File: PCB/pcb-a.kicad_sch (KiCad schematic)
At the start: 24 parts, among them Q3 BC337, Q4 BC337, SW1 config, U1 MCP23008-xP, U4 ATmega16L-8P, Y1 8Mhz

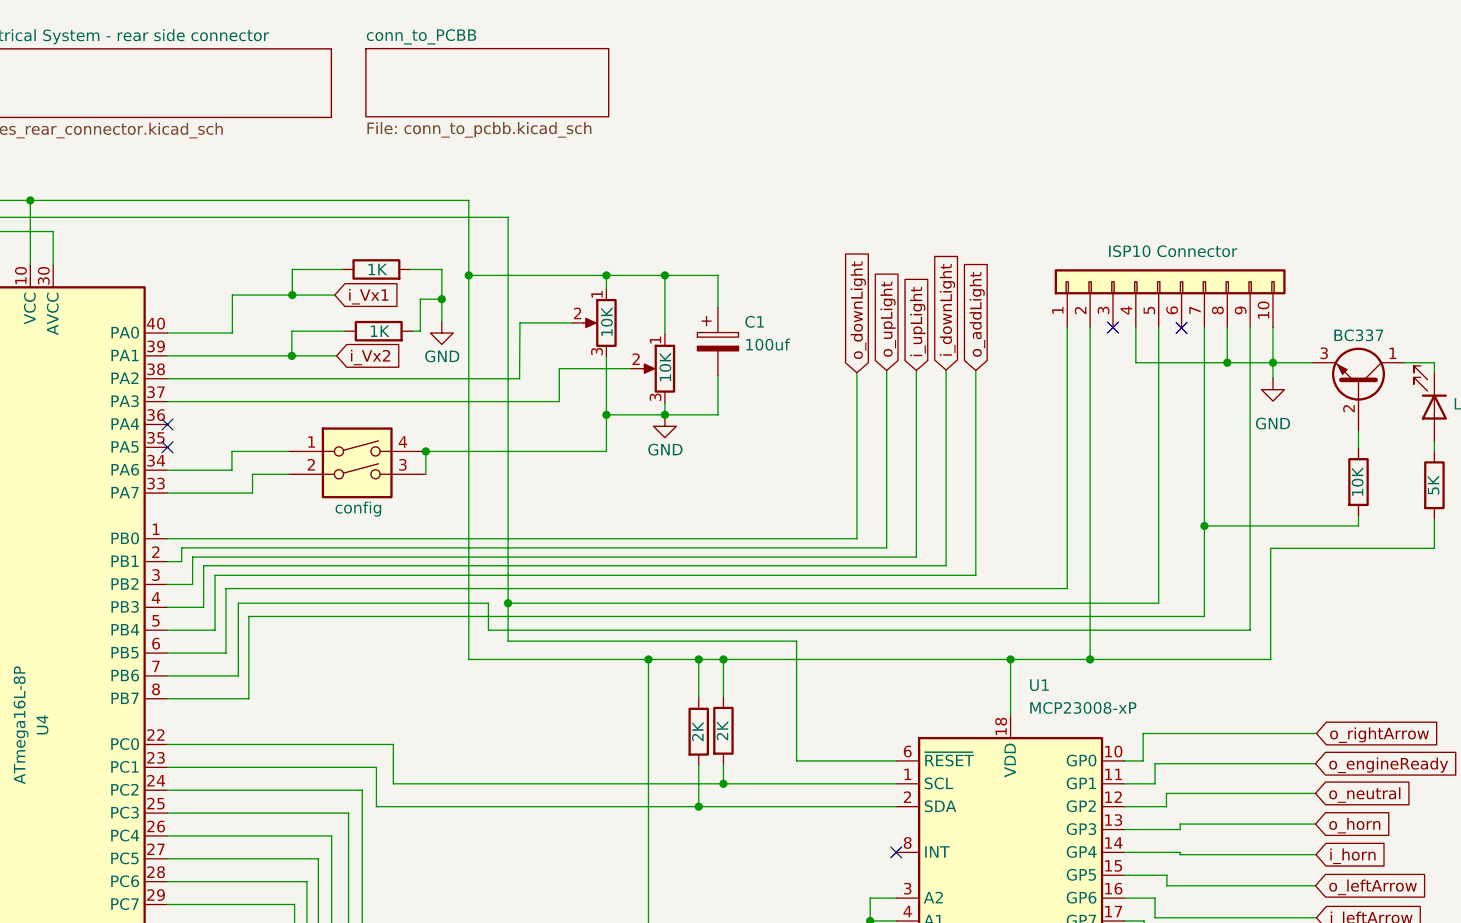
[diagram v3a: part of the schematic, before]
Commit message: Changes and porting to KiCAD-7.0
The MCP23008's reset PIN is no more connected to the MCU's reset. Now, it is connected to the A4 MCU's pin.
This change allows the MCU to reset the I2C connected device, when there are too many errors
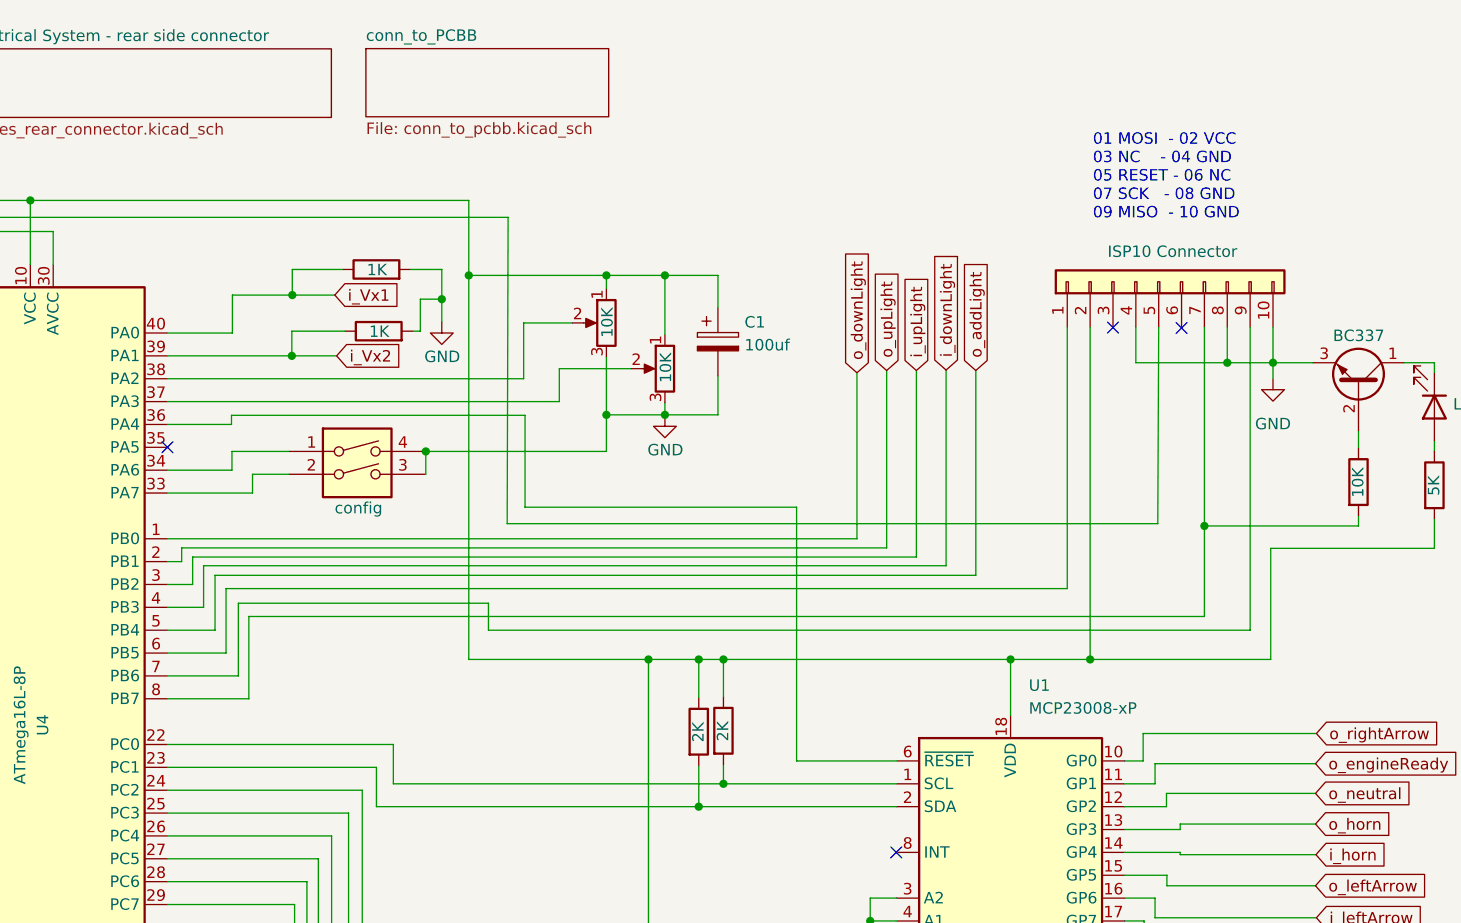
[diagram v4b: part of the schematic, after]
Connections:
- net i_powerOFF: no longer U1.6 (~{RESET})
- net at U4.36 (PA4): now also U1.6 (~{RESET})
- no-connect marks 7 -> 6
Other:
- note added: "01 MOSI - 02 VCC 03 NC - 04 GND 05 RESET - 06 NC 07 SCK - 08 GND 09 MISO - 10 GND"

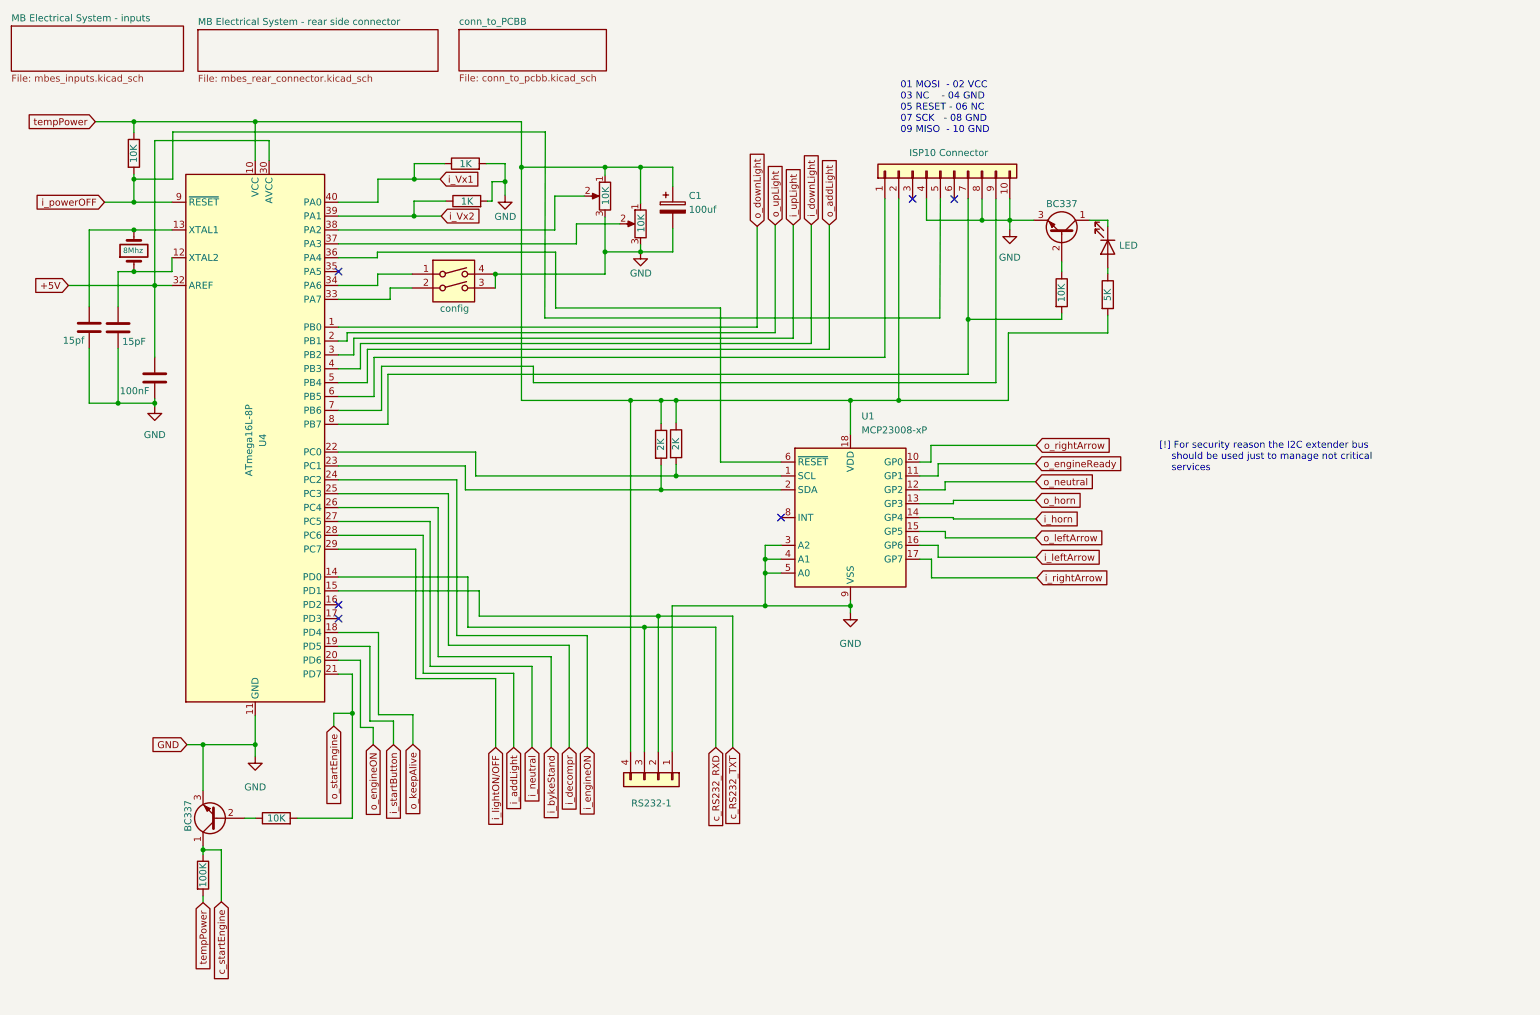
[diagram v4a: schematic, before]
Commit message: MAX232CPE added
In order to see the log messages when the device is mounted on motobike, I need to put the RS232 plug into the device directly.
For this reason I added the RS232 transciver to the circuit
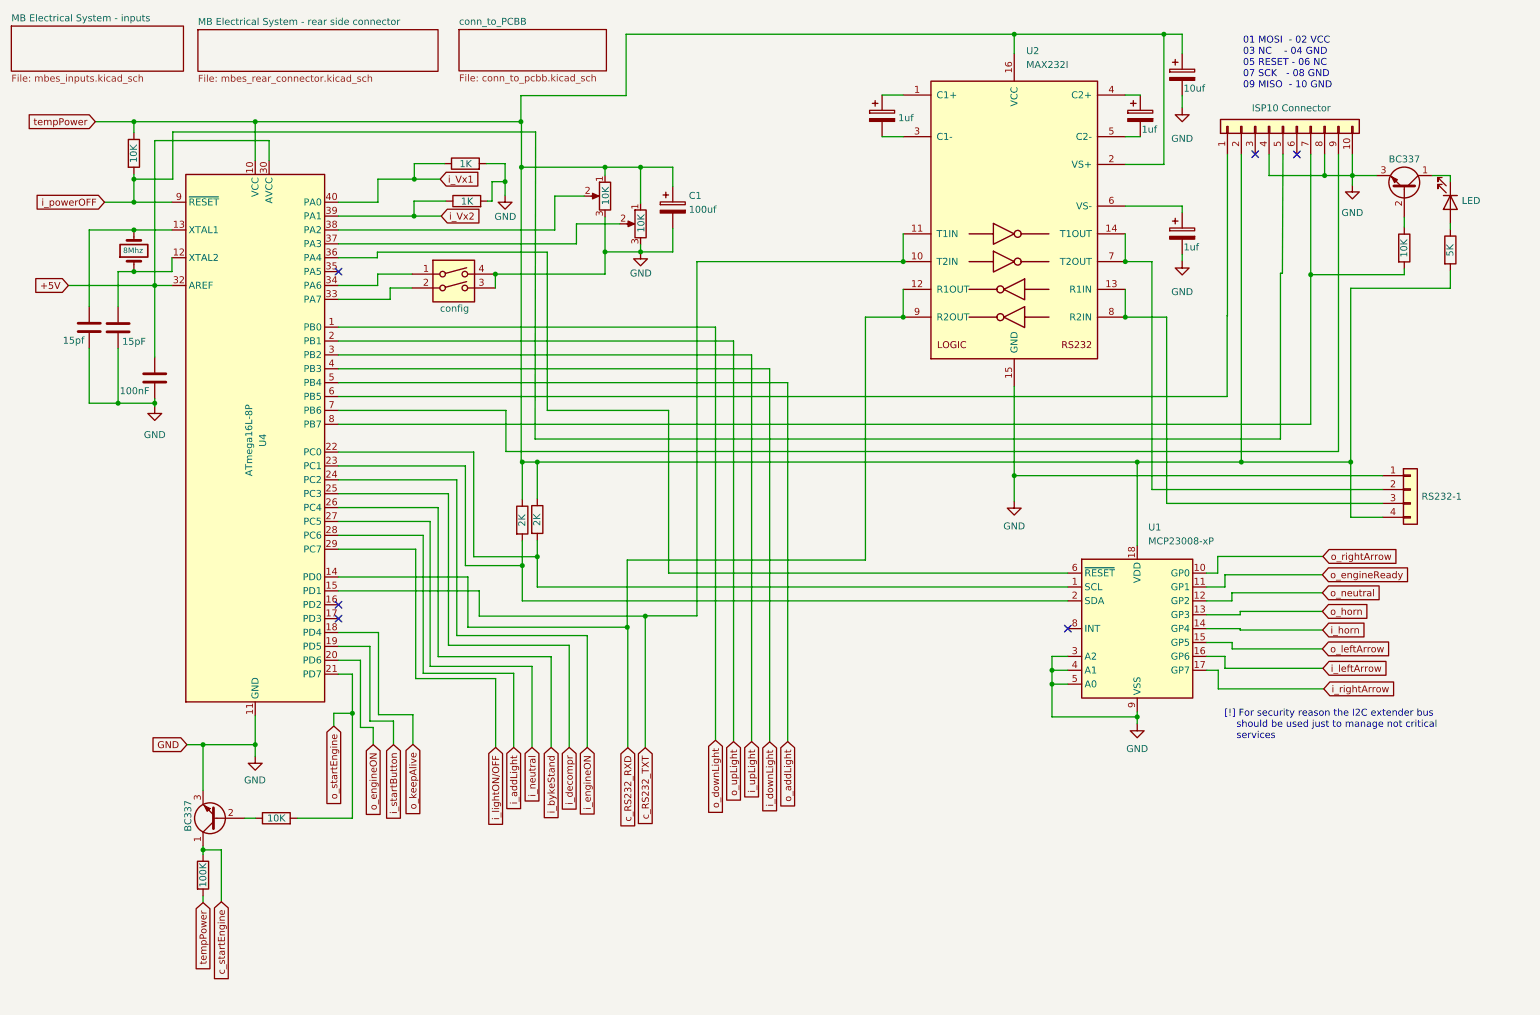
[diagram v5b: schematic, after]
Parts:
- added C5, C6, C8: 1uf, Capacitor_THT:CP_Radial_D8.0mm_P2.50mm, symbol Device:C_Polarized
- added C7: 10uf, Capacitor_THT:CP_Radial_D8.0mm_P2.50mm, symbol Device:C_Polarized
- added U2: MAX232I, symbol Interface_UART:MAX232I
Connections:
- net GND: now also C7.2, C8.2, U2.15 (GND)
- net c_RS232_RXD: now also U2.12 (R1OUT), U2.9 (R2OUT); no longer RS232-1.3 (Pin_3)
- net c_RS232_TXT: now also U2.10 (T2IN), U2.11 (T1IN); no longer RS232-1.2 (Pin_2)
- net tempPower: now also C7.1, U2.16 (VCC), U2.2 (VS+)
- new net: C5.1, U2.1 (C1+)
- new net: RS232-1.3 (Pin_3), U2.13 (R1IN), U2.8 (R2IN)
- new net: RS232-1.2 (Pin_2), U2.14 (T1OUT), U2.7 (T2OUT)
- new net: C5.2, U2.3 (C1-)
- new net: C6.1, U2.4 (C2+)
- new net: C6.2, U2.5 (C2-)
- new net: C8.1, U2.6 (VS-)
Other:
- moved on the sheet: RS232-1, U1

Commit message: MAX232CPE footprint added
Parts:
- U2: footprint (none) -> Package_DIP:CERDIP-16_W7.62mm_SideBrazed_LongPads
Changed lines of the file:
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@@
       (effects (font (size 1.27 1.27)) (justify left))
     )
-    (property "Footprint" "" (at 199.2376 79.9592 0)
+    (property "Footprint" "Package_DIP:CERDIP-16_W7.62mm_SideBrazed_LongPads" (at 199.2376 79.9592 0)
       (effects (font (size 1.27 1.27)) (justify left) hide)
     )

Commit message: Unresolved conflicts after the last marge
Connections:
- net c_RS232_RXD: no longer U2.12 (R1OUT)
- net c_RS232_TXT: no longer U2.11 (T1IN)
- net i_RPM: now reaches U4.16 (PD2)
- net i_odometer: now reaches U4.17 (PD3)
- net at SW1.2: now also ISP101.1 (Pin_1), U4.6 (PB5); no longer U4.33 (PA7)
- net at SW1.1: now also ISP101.9 (Pin_9), U4.7 (PB6); no longer U4.34 (PA6)
- net at RS232-1.3 (Pin_3), U2.8 (R2IN): no longer U2.13 (R1IN)
- net at RS232-1.2 (Pin_2), U2.7 (T2OUT): no longer U2.14 (T1OUT)
- new net i_temp1: U4.33 (PA7)
- new net i_temp2: U4.34 (PA6)
- no-connect marks 6 -> 4

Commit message: Rollback
It will be the last version using DIP. I have to accept it is an old technology, this PCB would be a great result in the 2000 age
but a century quarter is past! :-( It is the SMD age, now. So, after the second upograde of my laboratory,  I will rebuild the
PCB using SMDs.
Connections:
- net at ISP101.1 (Pin_1), U4.6 (PB5): no longer SW1.2
- net at ISP101.9 (Pin_9), U4.7 (PB6): no longer SW1.1
- net i_RPM: no longer names the net of U4.16 (PD2)
- net i_odometer: no longer names the net of U4.17 (PD3)
- net i_temp1: no longer names the net of U4.33 (PA7)
- net i_temp1: now also SW1.2
- net i_temp2: no longer names the net of U4.34 (PA6)
- net i_temp2: now also SW1.1
- no-connect marks 4 -> 6
